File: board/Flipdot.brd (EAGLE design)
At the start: 154 x 85 mm, 36 parts, among them IC1 MAX7301AAX+, X1 AC 230 V

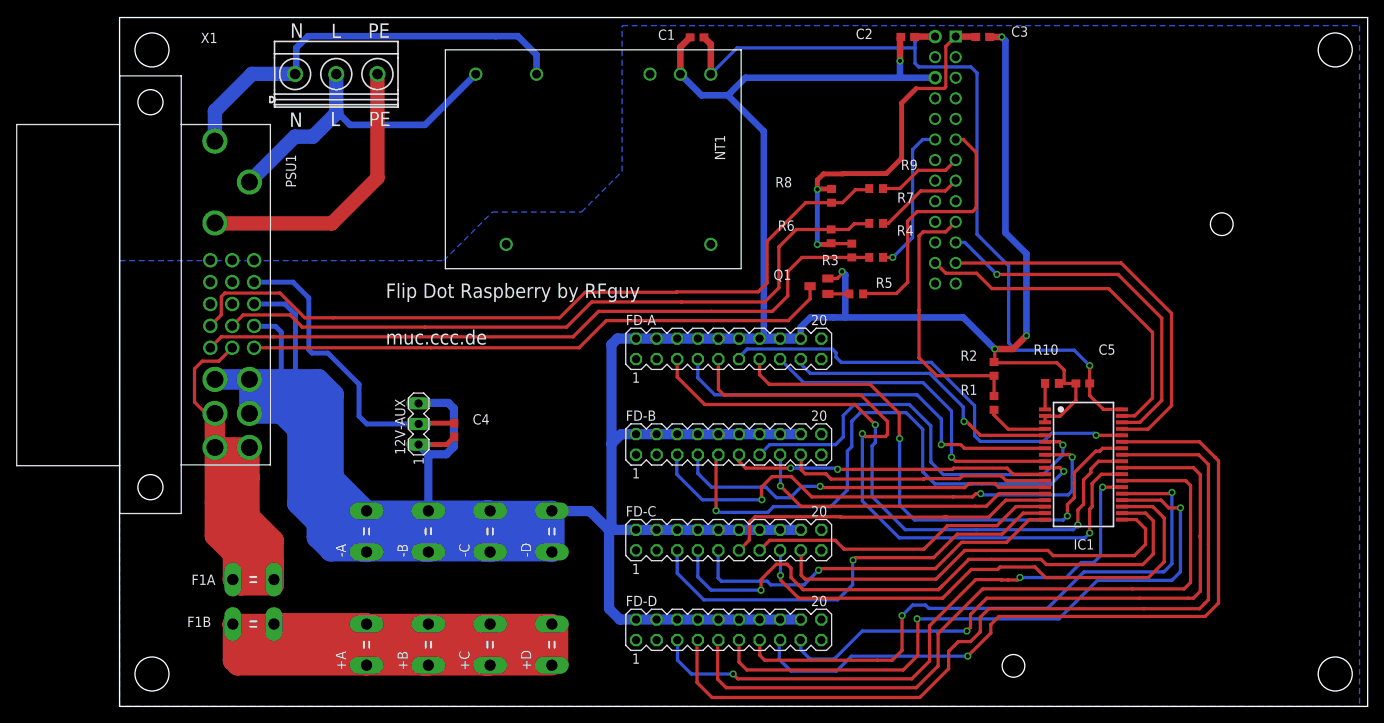
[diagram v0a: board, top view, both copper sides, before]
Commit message: fix(board): move gpio from pin 17 to pin 3
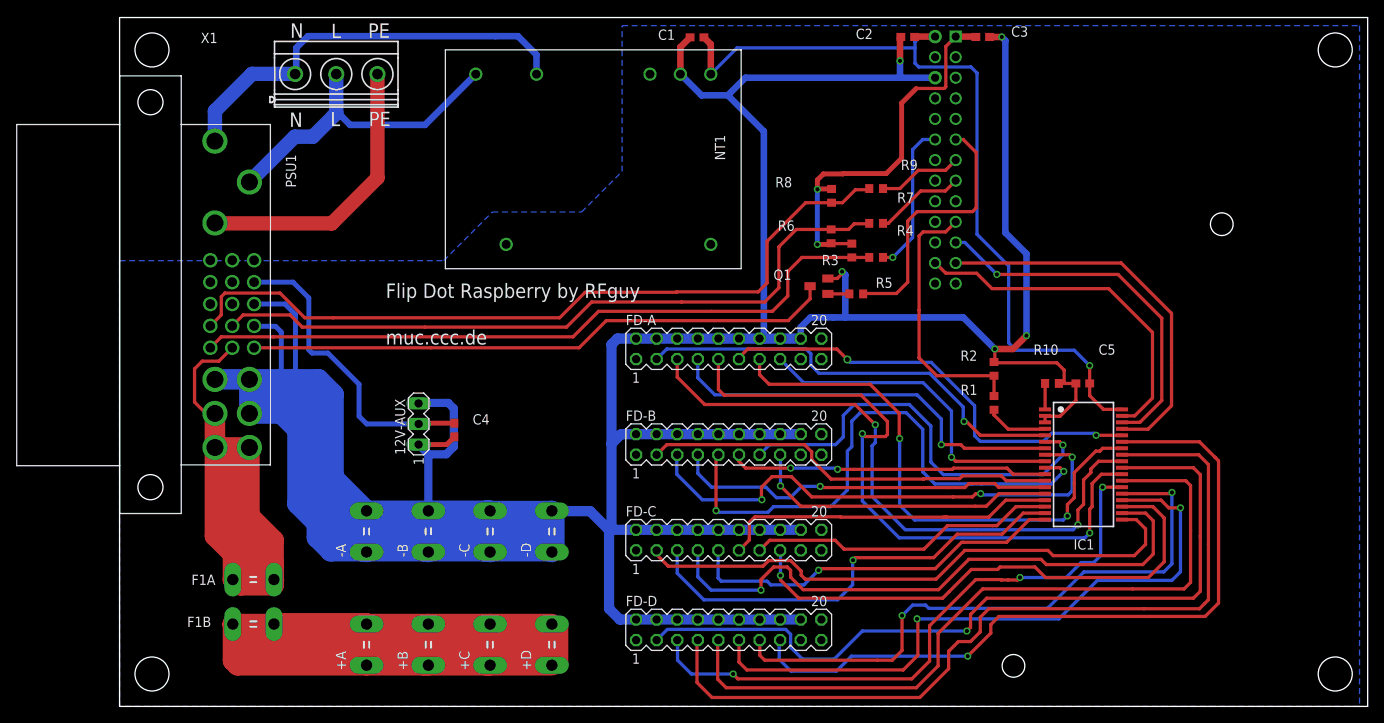
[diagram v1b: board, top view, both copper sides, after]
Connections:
- net N$10: now also FD-B.3; no longer FD-B.17
- net N$15: now also FD-C.3; no longer FD-C.17
- net N$20: now also FD-D.3; no longer FD-D.17
- net N$5: now also FD-A.3; no longer FD-A.17
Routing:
- net N$5: track 35.4 -> 54.7 mm
- net N$20: track 80.0 -> 98.9 mm
- net N$10: track 32.9 -> 51.2 mm
- net N$15: track 53.4 -> 70.6 mm
- net N$16: track 75.4 -> 74.4 mm
- net +24V: track 169.8 -> 169.0 mm
- net N$42: track 55.6 -> 55.3 mm, vias 1 -> 2
